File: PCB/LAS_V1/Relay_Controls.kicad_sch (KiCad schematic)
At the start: 11 parts, among them J3 Conn_01x06_Pin, K1 SANYOU_SRD_Form_C, K2 SANYOU_SRD_Form_A, Q1 NPN, U1 ULN2003A

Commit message: -am
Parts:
- removed D3: LED, symbol Device:LED
- removed J3: Conn_01x06_Pin, symbol Connector:Conn_01x06_Pin
- removed K2: SANYOU_SRD_Form_A, Relay_THT:Relay_SPST_SANYOU_SRD_Series_Form_A, symbol Relay:SANYOU_SRD_Form_A
- removed R3: R_Small_US, symbol Device:R_Small_US
- removed U1: ULN2003A, symbol Transistor_Array:ULN2003A

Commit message: installing JLB, PCB mostly done
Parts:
- R1: value R_Small_US -> 4.7k
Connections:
- net +12V renamed +5V
- net relay1 renamed relay_act
- net relay_input1 renamed COM
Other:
- moved on the sheet: D1, D2, K1, Q1, R1, R2

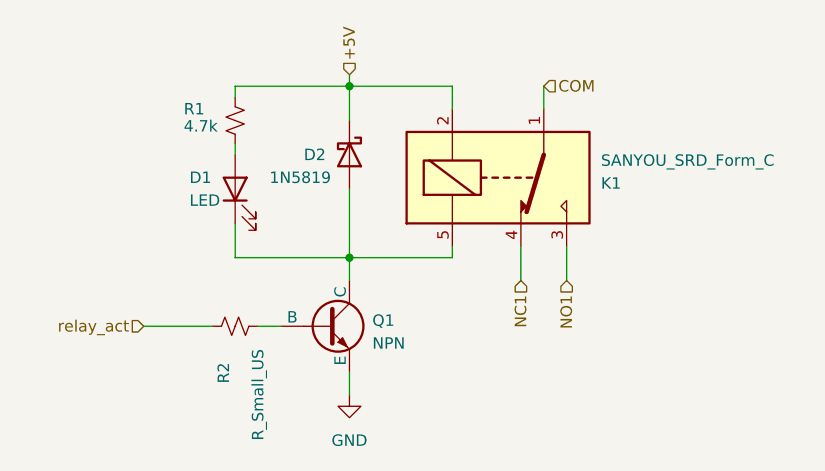
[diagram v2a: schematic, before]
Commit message: added JLBPCB part Numbers
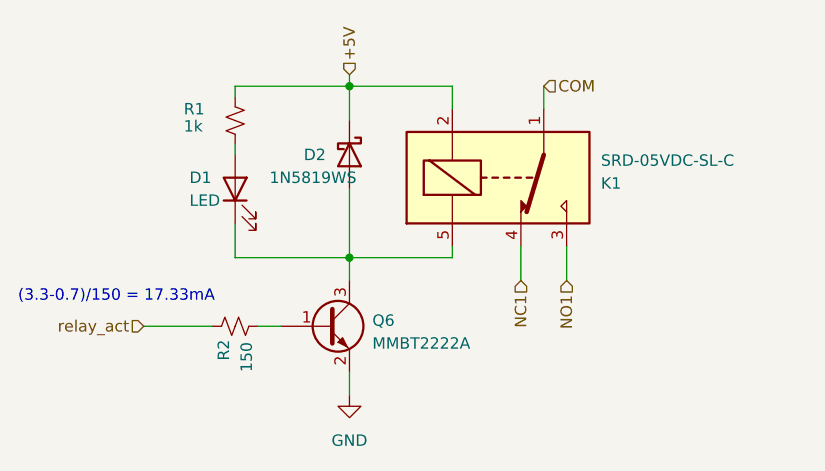
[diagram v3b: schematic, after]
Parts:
- removed Q1: NPN, symbol Simulation_SPICE:NPN
- added Q6: MMBT2222A, Package_TO_SOT_SMD:SOT-23, symbol Transistor_BJT:MMBT3904
- D1: footprint (none) -> LED_SMD:LED_0603_1608Metric; LCSC (none) -> C2286
- D2: value 1N5819 -> 1N5819WS; footprint Diode_THT:D_DO-41_SOD81_P10.16mm_Horizontal -> Diode_SMD:D_SOD-323; LCSC (none) -> C191023
- K1: value SANYOU_SRD_Form_C -> SRD-05VDC-SL-C; LCSC (none) -> C35449
- R1: value 4.7k -> 1k; footprint (none) -> Resistor_SMD:R_0603_1608Metric; LCSC (none) -> C21190
- R2: value R_Small_US -> 150; footprint (none) -> Resistor_SMD:R_0603_1608Metric; LCSC (none) -> C22808
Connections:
- net GND: now also Q6.2 (E)
- net at D1.1 (K), D2.2 (A), K1.5: now also Q6.3 (C)
- net at R2.2: now also Q6.1 (B)
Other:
- note added: "(3.3-0.7)/150 = 17.33mA"
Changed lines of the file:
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@@
     (stroke (width 0) (type default))
+  )
+  (text "(3.3-0.7)/150 = 17.33mA\n" (at 77.47 66.04 0)
+    (effects (font (size 1.27 1.27)) (justify left bottom))
   )
   (hierarchical_label "relay_act" (shape input) (at 91.44 68.58 180) (fields_autoplaced)
@@
       (effects (font (size 1.27 1.27)) (justify left))
     )
-    (property "Value" "1N5819" (at 105.41 52.07 90)
-      (effects (font (size 1.27 1.27)) (justify left))
-    )
-    (property "Footprint" "Diode_THT:D_DO-41_SOD81_P10.16mm_Horizontal" (at 109.855 49.53 0)
+    (property "Value" "1N5819WS" (at 105.41 52.07 90)
+      (effects (font (size 1.27 1.27)) (justify left))
+    )
+    (property "Footprint" "Diode_SMD:D_SOD-323" (at 109.855 49.53 0)
       (effects (font (size 1.27 1.27)) hide)
     )
@@
       (effects (font (size 1.27 1.27)) hide)
     )
-    (property "LCSC" "" (at 114.3 49.53 0)
+    (property "LCSC" "C191023" (at 114.3 49.53 0)
       (effects (font (size 1.27 1.27)) hide)
     )
@@
         )
         (path "/aadef4b8-3115-4a49-998f-828f2021a6b4/7898df78-2a61-4f8a-8974-01dfb9e5acb5"
-          (reference "#PWR018") (unit 1)
+          (reference "#PWR017") (unit 1)
         )
       )
@@
   (symbol (lib_id "Device:R_Small_US") (at 101.6 68.58 90) (unit 1)
     (in_bom yes) (on_board yes) (dnp no)
-    (property "Reference" "R2" (at 100.33 74.93 0)
-      (effects (font (size 1.27 1.27)) (justify left))
-    )
-    (property "Value" "R_Small_US" (at 104.14 81.28 0)
-      (effects (font (size 1.27 1.27)) (justify left))
-    )
-    (property "Footprint" "" (at 101.6 68.58 0)
+    (property "Reference" "R2" (at 100.33 72.39 0)
+      (effects (font (size 1.27 1.27)) (justify left))
+    )
+    (property "Value" "150" (at 102.87 73.66 0)
+      (effects (font (size 1.27 1.27)) (justify left))
+    )
+    (property "Footprint" "Resistor_SMD:R_0603_1608Metric" (at 101.6 68.58 0)
       (effects (font (size 1.27 1.27)) hide)
     )
@@
       (effects (font (size 1.27 1.27)) hide)
     )
-    (property "LCSC" "" (at 101.6 68.58 0)
+    (property "LCSC" "C22808" (at 101.6 68.58 0)
       (effects (font (size 1.27 1.27)) hide)
     )
@@
     )
   )
-  (symbol (lib_id "Simulation_SPICE:NPN") (at 111.76 68.58 0) (unit 1)
+  (symbol (lib_id "Transistor_BJT:MMBT3904") (at 111.76 68.58 0) (unit 1)
     (in_bom yes) (on_board yes) (dnp no) (fields_autoplaced)
-    (property "Reference" "Q1" (at 116.84 67.945 0)
-      (effects (font (size 1.27 1.27)) (justify left))
-    )
-    (property "Value" "NPN" (at 116.84 70.485 0)
-      (effects (font (size 1.27 1.27)) (justify left))
-    )
-    (property "Footprint" "" (at 175.26 68.58 0)
-      (effects (font (size 1.27 1.27)) hide)
-    )
-    (property "Datasheet" "~" (at 175.26 68.58 0)
-      (effects (font (size 1.27 1.27)) hide)
-    )
-    (property "Sim.Device" "NPN" (at 111.76 68.58 0)
-      (effects (font (size 1.27 1.27)) hide)
-    )
-    (property "Sim.Type" "GUMMELPOON" (at 111.76 68.58 0)
-      (effects (font (size 1.27 1.27)) hide)
-    )
-    (property "Sim.Pins" "1=C 2=B 3=E" (at 111.76 68.58 0)
-      (effects (font (size 1.27 1.27)) hide)
-    )
-    (property "LCSC" "" (at 111.76 68.58 0)
+    (property "Reference" "Q6" (at 116.84 67.945 0)
+      (effects (font (size 1.27 1.27)) (justify left))
+    )
+    (property "Value" "MMBT2222A" (at 116.84 70.485 0)
+      (effects (font (size 1.27 1.27)) (justify left))
+    )
+    (property "Footprint" "Package_TO_SOT_SMD:SOT-23" (at 116.84 70.485 0)
+      (effects (font (size 1.27 1.27) italic) (justify left) hide)
+    )
+    (property "Datasheet" "https://www.onsemi.com/pub/Collateral/2N3903-D.PDF" (at 111.76 68.58 0)
+      (effects (font (size 1.27 1.27)) (justify left) hide)
+    )
+    (property "LCSC" "C8512" (at 111.76 68.58 0)
       (effects (font (size 1.27 1.27)) hide)
     )
@@
     (instances
       (project "LAS_V1"
-        (path "/aadef4b8-3115-4a49-998f-828f2021a6b4"
+        (path "/aadef4b8-3115-4a49-998f-828f2021a6b4/a475df9f-c6e9-4f77-bf99-c031d1147f10"
+          (reference "Q6") (unit 1)
+        )
+        (path "/aadef4b8-3115-4a49-998f-828f2021a6b4/7898df78-2a61-4f8a-8974-01dfb9e5acb5"
           (reference "Q1") (unit 1)
         )
-        (path "/aadef4b8-3115-4a49-998f-828f2021a6b4/7898df78-2a61-4f8a-8974-01dfb9e5acb5"
-          (reference "Q1") (unit 1)
-        )
       )
     )
@@
       (effects (font (size 1.27 1.27)) (justify left))
     )
-    (property "Value" "SANYOU_SRD_Form_C" (at 142.24 50.165 0)
+    (property "Value" "SRD-05VDC-SL-C" (at 142.24 50.165 0)
       (effects (font (size 1.27 1.27)) (justify left))
     )
@@
       (effects (font (size 1.27 1.27)) hide)
     )
-    (property "LCSC" "" (at 130.81 52.07 0)
+    (property "LCSC" "C35449" (at 130.81 52.07 0)
       (effects (font (size 1.27 1.27)) hide)
     )
@@
       (effects (font (size 1.27 1.27)) (justify right))
     )
-    (property "Footprint" "" (at 101.6 53.34 0)
+    (property "Footprint" "LED_SMD:LED_0603_1608Metric" (at 101.6 53.34 0)
       (effects (font (size 1.27 1.27)) hide)
     )
@@
       (effects (font (size 1.27 1.27)) hide)
     )
-    (property "LCSC" "" (at 101.6 53.34 0)
+    (property "LCSC" "C2286" (at 101.6 53.34 0)
       (effects (font (size 1.27 1.27)) hide)
     )
@@
       (effects (font (size 1.27 1.27)) (justify left))
     )
-    (property "Value" "4.7k" (at 95.885 46.355 0)
-      (effects (font (size 1.27 1.27)) (justify left))
-    )
-    (property "Footprint" "" (at 101.6 45.72 0)
+    (property "Value" "1k" (at 95.885 46.355 0)
+      (effects (font (size 1.27 1.27)) (justify left))
+    )
+    (property "Footprint" "Resistor_SMD:R_0603_1608Metric" (at 101.6 45.72 0)
       (effects (font (size 1.27 1.27)) hide)
     )
@@
       (effects (font (size 1.27 1.27)) hide)
     )
-    (property "LCSC" "" (at 101.6 45.72 0)
-      (effects (font (size 1.27 1.27)) hide)
-    )
+    (property "LCSC" "C21190" (at 101.6 45.72 0)
+      (effects (font (size 1.27 1.27)) hide)
+    )

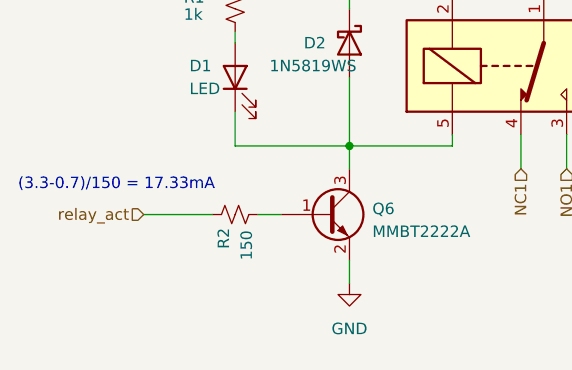
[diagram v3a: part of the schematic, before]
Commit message: All components Placed on PCB
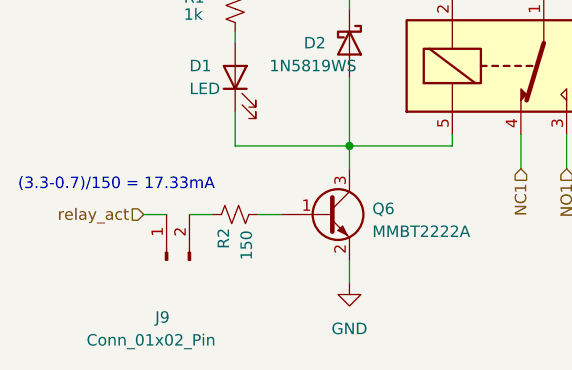
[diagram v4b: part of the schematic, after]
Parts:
- added J9: Conn_01x02_Pin, Connector_PinHeader_1.27mm:PinHeader_1x02_P1.27mm_Vertical, symbol Connector:Conn_01x02_Pin
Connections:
- net relay_act: now also J9.1 (Pin_1); no longer R2.1
- new net: J9.2 (Pin_2), R2.1
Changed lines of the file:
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@@
     (stroke (width 0) (type default))
   )
-  (wire (pts (xy 91.44 68.58) (xy 99.06 68.58))
+  (wire (pts (xy 96.52 68.58) (xy 99.06 68.58))
+    (stroke (width 0) (type default))
+  )
+  (wire (pts (xy 91.44 68.58) (xy 93.98 68.58))
     (stroke (width 0) (type default))
   )
@@
         )
         (path "/aadef4b8-3115-4a49-998f-828f2021a6b4/7898df78-2a61-4f8a-8974-01dfb9e5acb5"
-          (reference "D6") (unit 1)
+          (reference "D7") (unit 1)
         )
       )
@@
         )
         (path "/aadef4b8-3115-4a49-998f-828f2021a6b4/7898df78-2a61-4f8a-8974-01dfb9e5acb5"
-          (reference "#PWR017") (unit 1)
+          (reference "#PWR018") (unit 1)
         )
       )
@@
         )
         (path "/aadef4b8-3115-4a49-998f-828f2021a6b4/7898df78-2a61-4f8a-8974-01dfb9e5acb5"
-          (reference "R7") (unit 1)
+          (reference "R9") (unit 1)
         )
       )
@@
         )
         (path "/aadef4b8-3115-4a49-998f-828f2021a6b4/7898df78-2a61-4f8a-8974-01dfb9e5acb5"
-          (reference "D5") (unit 1)
+          (reference "D6") (unit 1)
+        )
+      )
+    )
+  )
+  (symbol (lib_id "Connector:Conn_01x02_Pin") (at 93.98 73.66 90) (unit 1)
+    (in_bom yes) (on_board yes) (dnp no)
+    (property "Reference" "J9" (at 92.71 80.01 90)
+      (effects (font (size 1.27 1.27)) (justify right))
+    )
+    (property "Value" "Conn_01x02_Pin" (at 85.09 82.55 90)
+      (effects (font (size 1.27 1.27)) (justify right))
+    )
+    (property "Footprint" "Connector_PinHeader_1.27mm:PinHeader_1x02_P1.27mm_Vertical" (at 93.98 73.66 0)
+      (effects (font (size 1.27 1.27)) hide)
+    )
+    (property "Datasheet" "~" (at 93.98 73.66 0)
+      (effects (font (size 1.27 1.27)) hide)
+    )
+    (pin "1")
+    (pin "2")
+    (instances
+      (project "LAS_V1"
+        (path "/aadef4b8-3115-4a49-998f-828f2021a6b4"
+          (reference "J9") (unit 1)
+        )
+        (path "/aadef4b8-3115-4a49-998f-828f2021a6b4/7898df78-2a61-4f8a-8974-01dfb9e5acb5"
+          (reference "J6") (unit 1)
         )
       )
@@
         )
         (path "/aadef4b8-3115-4a49-998f-828f2021a6b4/7898df78-2a61-4f8a-8974-01dfb9e5acb5"
-          (reference "R6") (unit 1)
-        )
-      )
+          (reference "R8") (unit 1)
+        )
+      )
